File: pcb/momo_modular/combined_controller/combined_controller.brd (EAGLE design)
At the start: 50.8 x 33 mm, 45 parts, among them Q1 32.768khz, Q2 P-MOSFET, U1 XRP7659, U2 PIC24FJ64GA306, U3 MCP1702, U5 FLASH8MSOP8, U6 MCP73811

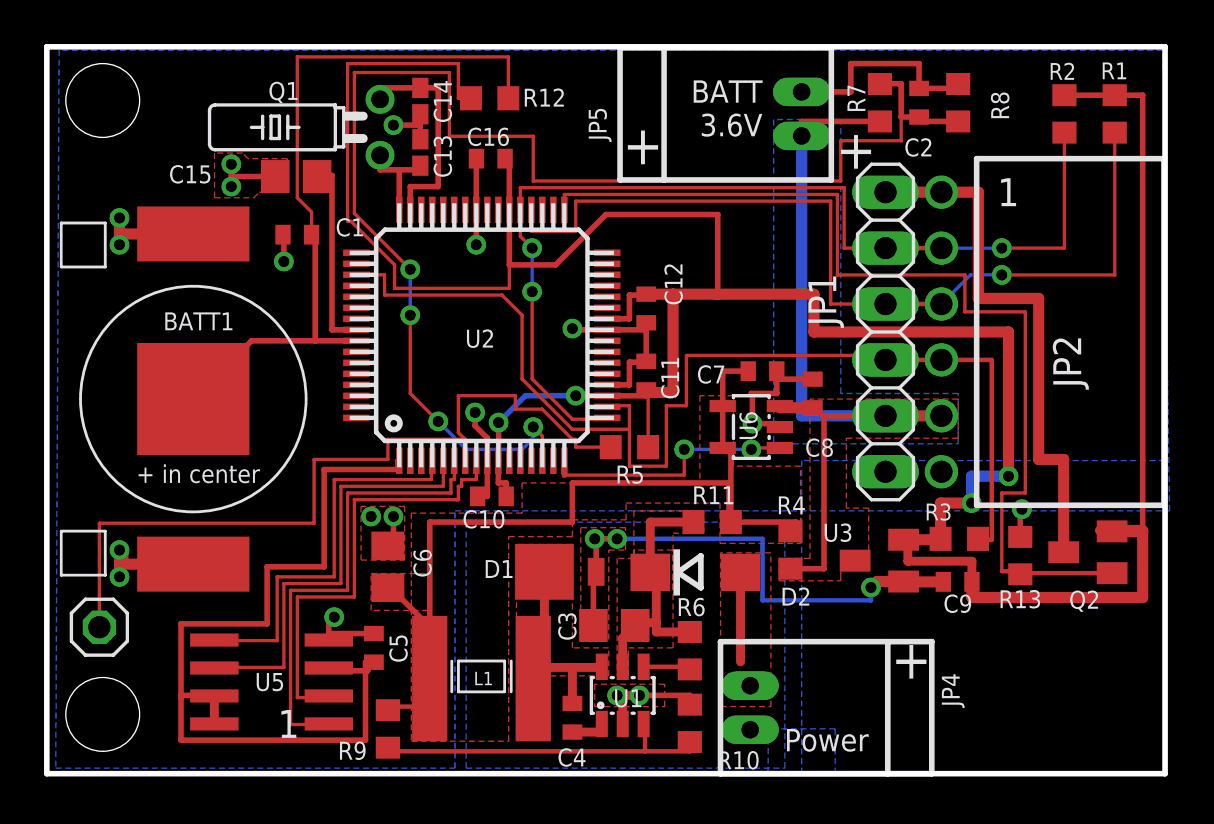
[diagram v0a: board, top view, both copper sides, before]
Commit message: Update Controller Board Layout
- add sense line for external power
- move components for easier placement
- reroute long lines
- flip backup battery orientation to allow for easy insertion
- move cap away from crystal to avoid shorts
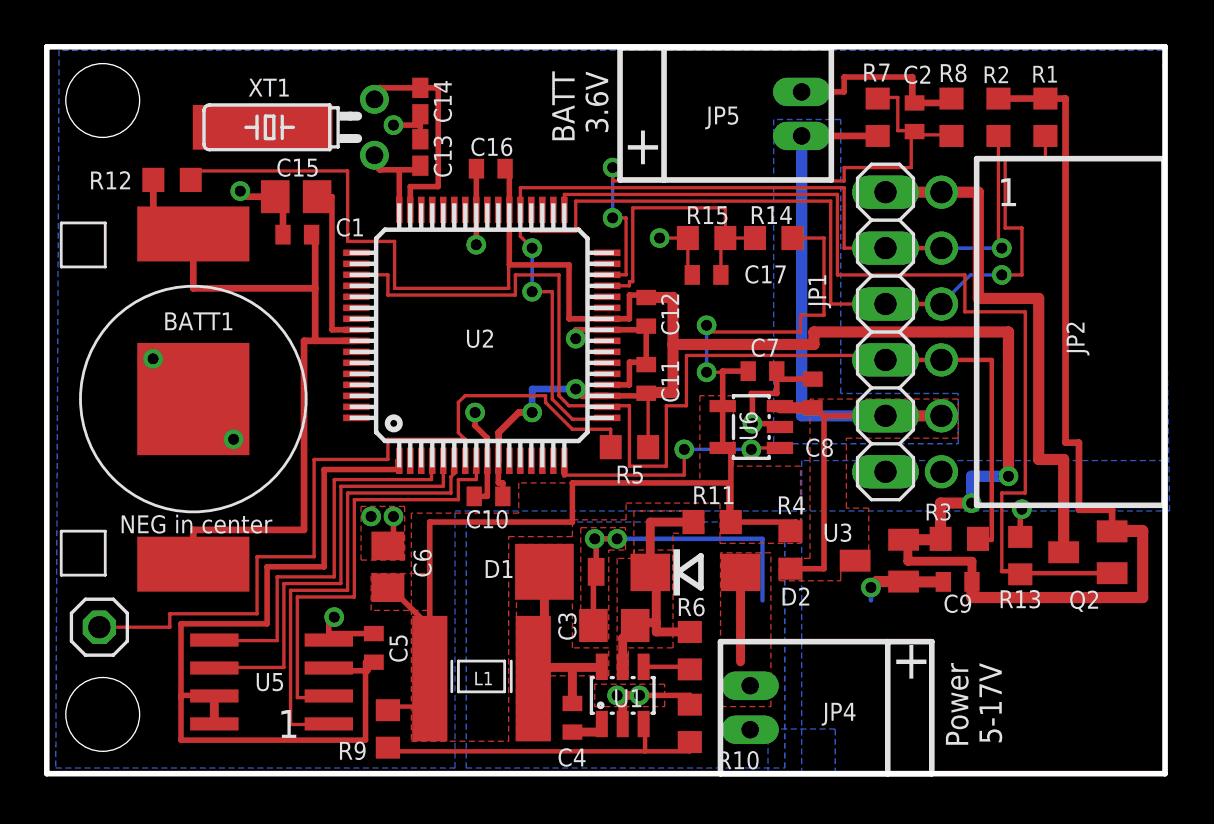
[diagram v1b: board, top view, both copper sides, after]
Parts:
- removed Q1: 32.768khz, crystal:TC26H
- added C17: 100 nF, rcl:C0402
- added R14, R15: 510K, rcl:R0603
- added XT1: 32.768khz, components:TC26H
- moved R12 14.9 mm to (39.7, 38.9), turned to 180 degrees
- moved R1 3.15 mm to (79.4, 41.8)
- moved R2 3.00 mm to (77.3, 41.8)
- moved C15 0.91 mm to (45.4, 38.2)
- moved R8 0.73 mm to (75.1, 41.8)
- moved C2 0.69 mm to (73.5, 41.8)
- moved R7 0.67 mm to (71.8, 41.8)
- moved C16 0.46 mm to (54.2, 39.4)
- moved C10 0.15 mm to (54.1, 24.5)
- moved C11 0.15 mm to (61.3, 29.9)
- moved C12 0.15 mm to (61.3, 32.9)
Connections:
- removed net N$5: C6.1, C7.1, L1.2, R11.2, R4.1, R9.2, U6.4, U6.5
- new net +5V: C6.1, C7.1, L1.2, R11.2, R14.2, R4.1, R9.2, U6.4, U6.5
- new net VEXT_SAMP: C17.1, R14.1, R15.2, U2.29
- net GND: now also BATT1.-, C17.2, R15.1; no longer BATT1.-1, BATT1.-2
- net N$6: now also XT1.2; no longer Q1.2
- net N$7: now also XT1.1; no longer Q1.1
- net VBAT: now also BATT1.+1, BATT1.+2; no longer BATT1.+
- net VBAT_SAMP: now also U2.30; no longer U2.14
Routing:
- net +5V: track 0.00 -> 59.1 mm, vias 0 -> 2
- net N$5: track 44.9 -> 0.00 mm
- net VBAT_SAMP: track 62.7 -> 28.2 mm, vias 4 -> 2
- net VEXT_SAMP: track 0.00 -> 13.5 mm
- net VCCINT: track 141.8 -> 130.2 mm
- net GND: track 84.9 -> 74.5 mm, vias 21 -> 18
- net ICLK: track 45.8 -> 43.5 mm
- net VBAT: track 33.3 -> 35.4 mm
- net IDAT: track 40.6 -> 38.8 mm
- net IRQ: track 51.9 -> 53.3 mm
- net VCAP: track 8.85 -> 7.83 mm
- net V+: track 36.9 -> 36.2 mm
- added copper zone on layer 1, net +5V
- removed copper zone on layer 1, net N$5
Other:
- board text added: "NEG in center"
- board text added: "Power 5-17V"
- board text removed: "+ in center"
- board text removed: "Power"
